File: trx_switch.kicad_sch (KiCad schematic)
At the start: 21 parts, among them U1801 AS169-73, U1802 AS169-73

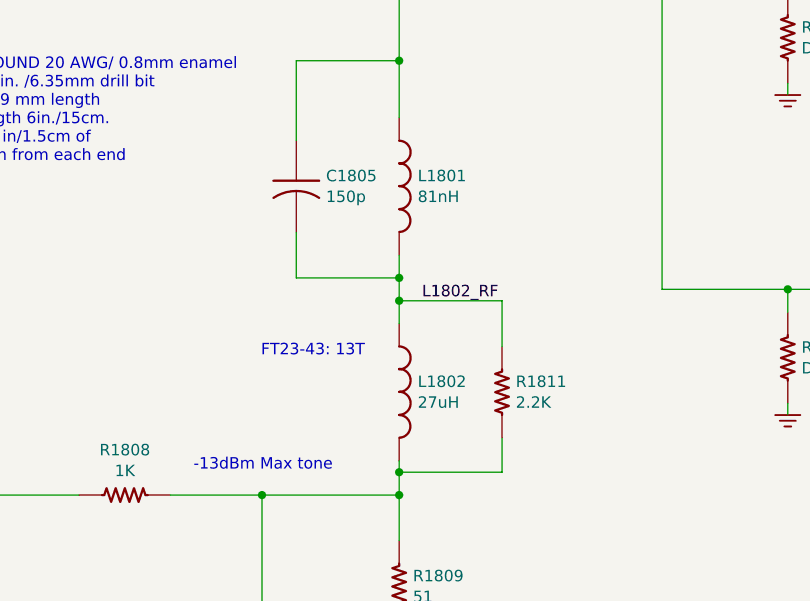
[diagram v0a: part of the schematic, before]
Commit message: Update pcb database to version 6
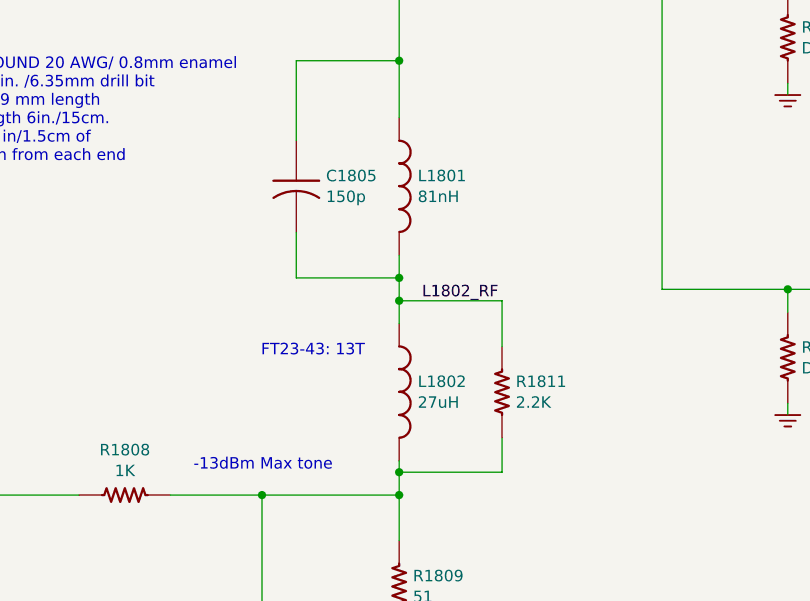
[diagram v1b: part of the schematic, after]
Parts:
- C1801, C1804: symbol Custom:C_US_0805_0.1UF_X7R_10%_50V_HS -> custom:C_US_0805_0.1UF_X7R_10%_50V_HS
- C1802: symbol Custom:C_US_0805_0.1UF_X7R_10%_50V_HS -> custom:C_US_0805_0.1UF_X7R_10%_50V_HS; PartNumber 800238-103 -> 800238-104
- C1803: symbol Custom:C_US_0805_0.1UF_X7R_10%_50V_HS -> custom:C_US_0805_0.1UF_X7R_10%_50V_HS; PartNumber 800239-102 -> 800238-104
- C1805: symbol Custom:C_US_0805_0.1UF_X7R_10%_50V_HS -> custom:C_US_0805_0.1UF_X7R_10%_50V_HS; PartNumber 800239-151 -> 800238-104
- L1801: symbol Custom:L_US -> custom:L_US; PartNumber 800YYY-YYY -> 8000XX-XXX
- L1802: symbol Custom:L_US -> custom:L_US; PartNumber 800257-023 -> 8000XX-XXX
- R1801, R1805: symbol Custom:R_US -> custom:R_US; PartNumber 800235-000 -> 800XXX-XXX
- R1802, R1803, R1806, R1807: symbol Custom:R_US -> custom:R_US
- R1804, R1809: symbol Custom:R_US_0805_1%_HS -> custom:R_US_0805_1%_HS; PartNumber 800235-510 -> 800235-XXX
- R1808, R1810: symbol Custom:R_US_0805_1%_HS -> custom:R_US_0805_1%_HS; PartNumber 800235-102 -> 800235-XXX
- R1811: symbol Custom:R_US -> custom:R_US; PartNumber 800235-222 -> 800XXX-XXX
- TP1801: symbol Custom:TESTPINTPSQ025 -> custom:TESTPINTPSQ025
- U1801, U1802: symbol Custom:AS169-73 -> custom:AS169-73

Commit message: Fix BOM part number errors and out of sync footprints which happened during conversion from Kicad 5 to 6
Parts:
- C1801, C1802, C1803: PartNumber 800238-104 -> 800239-103
- C1805: PartNumber 800238-104 -> 800239-151
- R1801, R1805: PartNumber 800XXX-XXX -> 800235-000
- R1802, R1803, R1806, R1807: PartNumber 800XXX-XXX -> (none)
- R1804, R1809: PartNumber 800235-XXX -> 800235-510
- R1808, R1810: PartNumber 800235-XXX -> 800235-102
- R1811: PartNumber 800XXX-XXX -> 800235-222
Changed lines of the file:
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@@
       (effects (font (size 1.524 1.524)))
     )
-    (property "PartNumber" "800235-XXX" (id 4) (at 165.862 144.78 90)
+    (property "PartNumber" "800235-510" (id 4) (at 165.862 144.78 90)
       (effects (font (size 1.524 1.524)) hide)
     )
@@
       (effects (font (size 1.524 1.524)))
     )
-    (property "PartNumber" "800238-104" (id 4) (at 161.29 52.07 0)
+    (property "PartNumber" "800239-103" (id 4) (at 161.29 52.07 0)
       (effects (font (size 1.524 1.524)) hide)
     )
@@
       (effects (font (size 1.524 1.524)))
     )
-    (property "PartNumber" "800238-104" (id 4) (at 220.98 44.45 0)
+    (property "PartNumber" "800239-103" (id 4) (at 220.98 44.45 0)
       (effects (font (size 1.524 1.524)) hide)
     )
@@
       (effects (font (size 1.524 1.524)))
     )
-    (property "PartNumber" "800238-104" (id 4) (at 138.43 48.26 0)
+    (property "PartNumber" "800239-103" (id 4) (at 138.43 48.26 0)
       (effects (font (size 1.524 1.524)) hide)
     )
@@
       (effects (font (size 1.524 1.524)))
     )
-    (property "PartNumber" "800235-XXX" (id 4) (at 62.992 110.49 90)
+    (property "PartNumber" "800235-510" (id 4) (at 62.992 110.49 90)
       (effects (font (size 1.524 1.524)) hide)
     )
@@
       (effects (font (size 1.524 1.524)))
     )
-    (property "PartNumber" "800235-XXX" (id 4) (at 133.35 141.732 90)
+    (property "PartNumber" "800235-102" (id 4) (at 133.35 141.732 90)
       (effects (font (size 1.524 1.524)) hide)
     )
@@
       (effects (font (size 1.524 1.524)))
     )
-    (property "PartNumber" "800235-XXX" (id 4) (at 133.35 187.452 90)
+    (property "PartNumber" "800235-102" (id 4) (at 133.35 187.452 90)
       (effects (font (size 1.524 1.524)) hide)
     )
@@
       (effects (font (size 1.524 1.524)))
     )
-    (property "PartNumber" "800XXX-XXX" (id 4) (at 224.282 119.38 90)
+    (property "PartNumber" "" (id 4) (at 224.282 119.38 90)
       (effects (font (size 1.524 1.524)) hide)
     )
@@
       (effects (font (size 1.524 1.524)))
     )
-    (property "PartNumber" "800XXX-XXX" (id 4) (at 209.042 119.38 90)
+    (property "PartNumber" "" (id 4) (at 209.042 119.38 90)
       (effects (font (size 1.524 1.524)) hide)
     )
@@
       (effects (font (size 1.524 1.524)))
     )
-    (property "PartNumber" "800XXX-XXX" (id 4) (at 214.63 118.872 90)
+    (property "PartNumber" "800235-000" (id 4) (at 214.63 118.872 90)
       (effects (font (size 1.524 1.524)) hide)
     )
@@
       (effects (font (size 1.524 1.524)))
     )
-    (property "PartNumber" "800XXX-XXX" (id 4) (at 224.282 83.82 90)
+    (property "PartNumber" "" (id 4) (at 224.282 83.82 90)
       (effects (font (size 1.524 1.524)) hide)
     )
@@
       (effects (font (size 1.524 1.524)))
     )
-    (property "PartNumber" "800XXX-XXX" (id 4) (at 209.042 83.82 90)
+    (property "PartNumber" "" (id 4) (at 209.042 83.82 90)
       (effects (font (size 1.524 1.524)) hide)
     )
@@
       (effects (font (size 1.524 1.524)))
     )
-    (property "PartNumber" "800XXX-XXX" (id 4) (at 214.63 83.312 90)
+    (property "PartNumber" "800235-000" (id 4) (at 214.63 83.312 90)
       (effects (font (size 1.524 1.524)) hide)
     )
@@
       (effects (font (size 1.524 1.524)))
     )
-    (property "PartNumber" "800XXX-XXX" (id 4) (at 177.292 123.19 90)
+    (property "PartNumber" "800235-222" (id 4) (at 177.292 123.19 90)
       (effects (font (size 1.524 1.524)) hide)
     )
@@
       (effects (font (size 1.524 1.524)))
     )
-    (property "PartNumber" "800238-104" (id 4) (at 149.86 88.9 0)
-      (effects (font (size 1.524 1.524)) hide)
-    )
+    (property "PartNumber" "800239-151" (id 4) (at 149.86 88.9 0)
+      (effects (font (size 1.524 1.524)) hide)
+    )

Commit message: trx_mobo_concept_2_B. Change design to use a dedicated 8V supply for the 2SC3357 parts. Add S-Meter connector. Change mic connector to 3 pins and add 8V sopower supply to pin 3.
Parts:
- removed R1810: 1K, Resistor_SMD:R_0805_2012Metric_Pad1.15x1.40mm_HandSolder, symbol custom:R_US_0805_1%_HS
- removed TP1801: TESTPINTPSQ025, mods:TESTPIN, symbol custom:TESTPINTPSQ025
- C1001: renamed from C1801; value 0.01u -> (none); footprint Capacitor_SMD:C_0805_2012Metric_Pad1.15x1.40mm_HandSolder -> (none)
- C1002: renamed from C1802; value 0.01u -> (none); footprint Capacitor_SMD:C_0805_2012Metric_Pad1.15x1.40mm_HandSolder -> (none)
- C1003: renamed from C1803; value 1000p -> (none); footprint Capacitor_SMD:C_0805_2012Metric_Pad1.15x1.40mm_HandSolder -> (none); PartNumber 800239-103 -> 800239-102
- C1004: renamed from C1804; value 0.1u -> (none); footprint Capacitor_SMD:C_0805_2012Metric_Pad1.15x1.40mm_HandSolder -> (none)
- C1005: renamed from C1805; value 150p -> (none); footprint Capacitor_SMD:C_0805_2012Metric_Pad1.15x1.40mm_HandSolder -> (none)
- L1001: renamed from L1801; value 81nH -> (none); footprint mods:AIR_CORE_9MMX6.3MM -> (none); PartNumber 8000XX-XXX -> 8XXXXX-XXX
- L1002: renamed from L1802; value 27uH -> (none); footprint mods:TOROID_T37_VERT -> (none); PartNumber 8000XX-XXX -> 800257-023
- R1001: renamed from R1801; value 0 -> (none); footprint Resistor_SMD:R_0805_2012Metric_Pad1.15x1.40mm_HandSolder -> (none)
- R1002: renamed from R1802; value DNI -> (none); footprint Resistor_SMD:R_0805_2012Metric_Pad1.15x1.40mm_HandSolder -> (none); PartNumber (none) -> 800XXX-XXX
- R1003: renamed from R1803; value DNI -> (none); footprint Resistor_SMD:R_0805_2012Metric_Pad1.15x1.40mm_HandSolder -> (none); PartNumber (none) -> 800XXX-XXX
- R1004: renamed from R1804; value 51 -> (none); footprint Resistor_SMD:R_0805_2012Metric_Pad1.15x1.40mm_HandSolder -> (none)
- R1005: renamed from R1805; value 0 -> (none); footprint Resistor_SMD:R_0805_2012Metric_Pad1.15x1.40mm_HandSolder -> (none)
- R1006: renamed from R1806; value DNI -> (none); footprint Resistor_SMD:R_0805_2012Metric_Pad1.15x1.40mm_HandSolder -> (none); PartNumber (none) -> 800XXX-XXX
- R1007: renamed from R1807; value DNI -> (none); footprint Resistor_SMD:R_0805_2012Metric_Pad1.15x1.40mm_HandSolder -> (none); PartNumber (none) -> 800XXX-XXX
- R1008: renamed from R1811; value 2.2K -> (none); footprint Resistor_SMD:R_0805_2012Metric_Pad1.15x1.40mm_HandSolder -> (none)
- R1009: renamed from R1808; value 1K -> (none); footprint Resistor_SMD:R_0805_2012Metric_Pad1.15x1.40mm_HandSolder -> (none)
- R1010: renamed from R1809; value 51 -> (none); footprint Resistor_SMD:R_0805_2012Metric_Pad1.15x1.40mm_HandSolder -> (none)
- U1001: renamed from U1801; value AS169-73 -> (none); footprint Package_TO_SOT_SMD:SOT-23-6_Handsoldering -> (none)
- U1002: renamed from U1802; value AS169-73 -> (none); footprint Package_TO_SOT_SMD:SOT-23-6_Handsoldering -> (none)
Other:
- note added: "HANDWOUND 20 AWG/ 0.8mm bus wire 5T 0.25 in. /6.35mm drill bit 0.375 in/9 mm length Wire length 6in./15cm."
- note removed: "HANDWOUND 20 AWG/ 0.8mm enamel 5T 0.25 in. /6.35mm drill bit 0.375 in/9 mm length Wire length 6in./15cm. Strip 0.6 in/1.5cm of insulation from each end"
